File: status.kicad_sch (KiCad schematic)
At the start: 12 parts, among them U7 STP08CP05

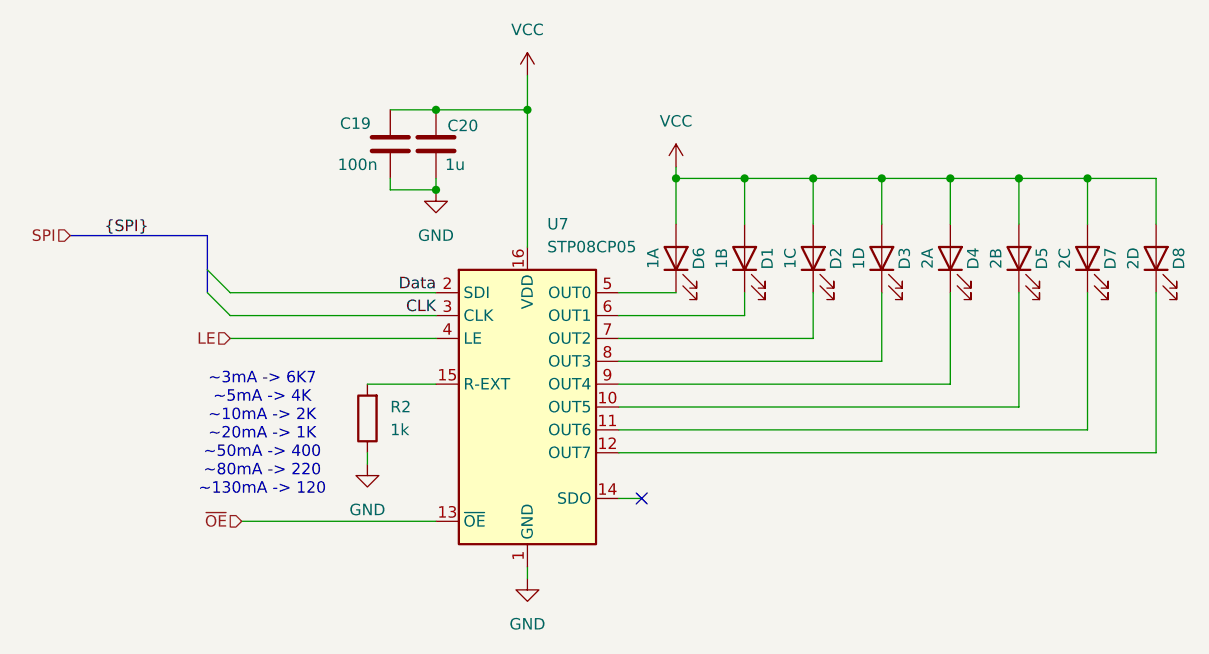
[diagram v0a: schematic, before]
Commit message: Resolve ERC warnings
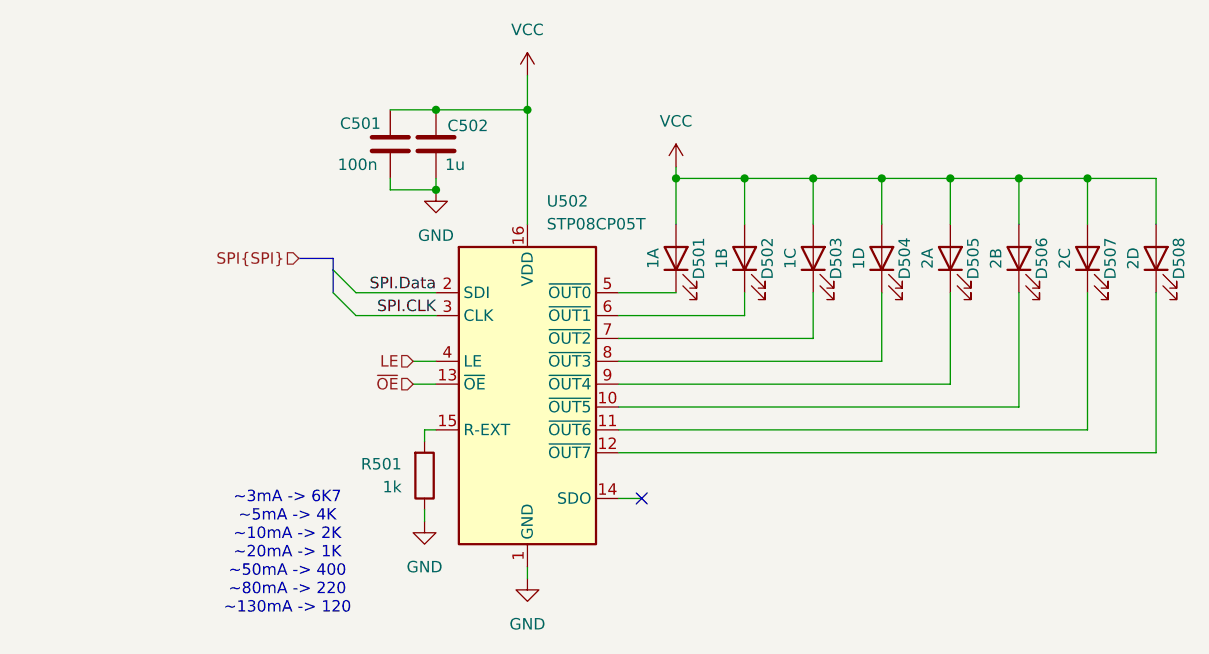
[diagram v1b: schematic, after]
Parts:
- removed U7: STP08CP05, symbol Driver_LED:STP08CP05
- added U502: STP08CP05T, Package_SO:TSSOP-16_4.4x5mm_P0.65mm, symbol Driver_LED:STP08CP05T
- renumbered C19 to C501, C20 to C502, D6 to D501, D1 to D502, D2 to D503, D3 to D504, D4 to D505, D5 to D506, D7 to D507, D8 to D508, R2 to R501
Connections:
- net GND: now also U502.1 (GND)
- net LE: now also U502.4 (LE)
- net VCC: now also U502.16 (VDD)
- net ~{OE}: now also U502.13 (~{OE})
- net at D501.1 (K): now also U502.5 (~{OUT0})
- net at D503.1 (K): now also U502.7 (~{OUT2})
- net at D508.1 (K): now also U502.12 (~{OUT7})
- net at D506.1 (K): now also U502.10 (~{OUT5})
- net at D504.1 (K): now also U502.8 (~{OUT3})
- net at D505.1 (K): now also U502.9 (~{OUT4})
- net at R501.2: now also U502.15 (R-EXT)
- net at D507.1 (K): now also U502.11 (~{OUT6})
- net at D502.1 (K): now also U502.6 (~{OUT1})
- new net SPI.CLK: U502.3 (CLK)
- new net SPI.Data: U502.2 (SDI)
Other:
- moved on the sheet: R501

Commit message: Add Testpoints
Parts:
- added TP12: LE, symbol Connector:TestPoint
- added TP13: ~{OE}, symbol Connector:TestPoint
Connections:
- net LE: now also TP12.1
- net ~{OE}: now also TP13.1
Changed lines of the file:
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@@
+	)
+	(junction
+		(at 110.49 96.52)
+		(diameter 0)
+		(color 0 0 0 0)
 	)
 	(junction
@@
 	)
 	(junction
+		(at 110.49 93.98)
+		(diameter 0)
+		(color 0 0 0 0)
+	)
+	(junction
 		(at 120.65 74.93)
 		(diameter 0)
@@
 	(wire
 		(pts
-			(xy 118.11 96.52) (xy 120.65 96.52)
+			(xy 107.95 96.52) (xy 110.49 96.52)
 		)
 		(stroke
@@
 	(wire
 		(pts
-			(xy 118.11 93.98) (xy 120.65 93.98)
+			(xy 107.95 93.98) (xy 110.49 93.98)
 		)
 		(stroke
@@
 	(wire
 		(pts
+			(xy 110.49 96.52) (xy 120.65 96.52)
+		)
+		(stroke
+			(width 0)
+			(type default)
+		)
+	)
+	(wire
+		(pts
 			(xy 119.38 101.6) (xy 120.65 101.6)
+		)
+		(stroke
+			(width 0)
+			(type default)
+		)
+	)
+	(wire
+		(pts
+			(xy 110.49 93.98) (xy 120.65 93.98)
 		)
 		(stroke
@@
 	(hierarchical_label "LE"
 		(shape input)
-		(at 118.11 93.98 180)
+		(at 107.95 93.98 180)
 		(effects
 			(font
@@
 	(hierarchical_label "~{OE}"
 		(shape input)
-		(at 118.11 96.52 180)
+		(at 107.95 96.52 180)
 		(effects
 			(font
@@
 	)
 	(symbol
+		(lib_id "Connector:TestPoint")
+		(at 110.49 93.98 0)
+		(unit 1)
+		(exclude_from_sim no)
+		(in_bom yes)
+		(on_board yes)
+		(dnp no)
+		(property "Reference" "TP12"
+			(at 112.014 90.424 0)
+			(effects
+				(font
+					(size 1.27 1.27)
+				)
+				(justify left)
+			)
+		)
+		(property "Value" "LE"
+			(at 112.268 92.71 0)
+			(effects
+				(font
+					(size 1.27 1.27)
+				)
+				(justify left)
+			)
+		)
+		(property "Footprint" ""
+			(at 115.57 93.98 0)
+			(effects
+				(font
+					(size 1.27 1.27)
+				)
+				(hide yes)
+			)
+		)
+		(property "Datasheet" "~"
+			(at 115.57 93.98 0)
+			(effects
+				(font
+					(size 1.27 1.27)
+				)
+				(hide yes)
+			)
+		)
+		(property "Description" "test point"
+			(at 110.49 93.98 0)
+			(effects
+				(font
+					(size 1.27 1.27)
+				)
+				(hide yes)
+			)
+		)
+		(pin "1"
+		)
+		(instances
+			(project "LifeCounter"
+				(path "/16b3e55a-9d75-49bf-a6fe-25414eb3d7da/8c2171b0-d87d-41f8-af80-94d86e99ac21"
+					(reference "TP12")
+					(unit 1)
+				)
+			)
+		)
+	)
+	(symbol
 		(lib_id "Device:LED")
 		(at 162.56 82.55 90)
@@
 					(unit 1)
 				)
+			)
+		)
+	)
+	(symbol
+		(lib_id "Connector:TestPoint")
+		(at 110.49 96.52 180)
+		(unit 1)
+		(exclude_from_sim no)
+		(in_bom yes)
+		(on_board yes)
+		(dnp no)
+		(fields_autoplaced yes)
+		(property "Reference" "TP13"
+			(at 113.03 98.5519 0)
+			(effects
+				(font
+					(size 1.27 1.27)
+				)
+				(justify right)
+			)
+		)
+		(property "Value" "~{OE}"
+			(at 113.03 101.0919 0)
+			(effects
+				(font
+					(size 1.27 1.27)
+				)
+				(justify right)
+			)
+		)
+		(property "Footprint" ""
+			(at 105.41 96.52 0)
+			(effects
+				(font
+					(size 1.27 1.27)
+				)
+				(hide yes)
+			)
+		)
+		(property "Datasheet" "~"
+			(at 105.41 96.52 0)
+			(effects
+				(font
+					(size 1.27 1.27)
+				)
+				(hide yes)
+			)
+		)
+		(property "Description" "test point"
+			(at 110.49 96.52 0)
+			(effects
+				(font
+					(size 1.27 1.27)
+				)
+				(hide yes)
+			)
+		)
+		(pin "1"
+		)
+		(instances
+			(project "LifeCounter"
+				(path "/16b3e55a-9d75-49bf-a6fe-25414eb3d7da/8c2171b0-d87d-41f8-af80-94d86e99ac21"
+					(reference "TP13")
+					(unit 1)
+				)

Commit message: Footprint selection
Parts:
- C501, C502: footprint Capacitor_SMD:C_0805_2012Metric_Pad1.18x1.45mm_HandSolder -> Capacitor_SMD:C_1206_3216Metric_Pad1.33x1.80mm_HandSolder
- D501, D502, D503, D504, D505, D506, D507, D508: footprint LED_SMD:LED_0805_2012Metric_Pad1.15x1.40mm_HandSolder -> LED_SMD:LED_1206_3216Metric_Pad1.42x1.75mm_HandSolder
- R501: footprint Resistor_SMD:R_0805_2012Metric_Pad1.20x1.40mm_HandSolder -> Resistor_SMD:R_1206_3216Metric_Pad1.30x1.75mm_HandSolder
- TP12, TP13: footprint (none) -> TestPoint:TestPoint_Pad_D1.0mm
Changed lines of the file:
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@@
 			)
 		)
-		(property "Footprint" "LED_SMD:LED_0805_2012Metric_Pad1.15x1.40mm_HandSolder"
+		(property "Footprint" "LED_SMD:LED_1206_3216Metric_Pad1.42x1.75mm_HandSolder"
 			(at 147.32 82.55 0)
 			(effects
@@
 			)
 		)
-		(property "Footprint" ""
+		(property "Footprint" "TestPoint:TestPoint_Pad_D1.0mm"
 			(at 115.57 93.98 0)
 			(effects
@@
 			)
 		)
-		(property "Footprint" "LED_SMD:LED_0805_2012Metric_Pad1.15x1.40mm_HandSolder"
+		(property "Footprint" "LED_SMD:LED_1206_3216Metric_Pad1.42x1.75mm_HandSolder"
 			(at 162.56 82.55 0)
 			(effects
@@
 			)
 		)
-		(property "Footprint" "Capacitor_SMD:C_0805_2012Metric_Pad1.18x1.45mm_HandSolder"
+		(property "Footprint" "Capacitor_SMD:C_1206_3216Metric_Pad1.33x1.80mm_HandSolder"
 			(at 121.6152 73.66 0)
 			(effects
@@
 			)
 		)
-		(property "Footprint" "LED_SMD:LED_0805_2012Metric_Pad1.15x1.40mm_HandSolder"
+		(property "Footprint" "LED_SMD:LED_1206_3216Metric_Pad1.42x1.75mm_HandSolder"
 			(at 200.66 82.55 0)
 			(effects
@@
 			)
 		)
-		(property "Footprint" "LED_SMD:LED_0805_2012Metric_Pad1.15x1.40mm_HandSolder"
+		(property "Footprint" "LED_SMD:LED_1206_3216Metric_Pad1.42x1.75mm_HandSolder"
 			(at 185.42 82.55 0)
 			(effects
@@
 			)
 		)
-		(property "Footprint" "LED_SMD:LED_0805_2012Metric_Pad1.15x1.40mm_HandSolder"
+		(property "Footprint" "LED_SMD:LED_1206_3216Metric_Pad1.42x1.75mm_HandSolder"
 			(at 170.18 82.55 0)
 			(effects
@@
 			)
 		)
-		(property "Footprint" "LED_SMD:LED_0805_2012Metric_Pad1.15x1.40mm_HandSolder"
+		(property "Footprint" "LED_SMD:LED_1206_3216Metric_Pad1.42x1.75mm_HandSolder"
 			(at 177.8 82.55 0)
 			(effects
@@
 			)
 		)
-		(property "Footprint" "Resistor_SMD:R_0805_2012Metric_Pad1.20x1.40mm_HandSolder"
+		(property "Footprint" "Resistor_SMD:R_1206_3216Metric_Pad1.30x1.75mm_HandSolder"
 			(at 117.602 106.68 90)
 			(effects
@@
 			)
 		)
-		(property "Footprint" ""
+		(property "Footprint" "TestPoint:TestPoint_Pad_D1.0mm"
 			(at 105.41 96.52 0)
 			(effects
@@
 			)
 		)
-		(property "Footprint" "LED_SMD:LED_0805_2012Metric_Pad1.15x1.40mm_HandSolder"
+		(property "Footprint" "LED_SMD:LED_1206_3216Metric_Pad1.42x1.75mm_HandSolder"
 			(at 193.04 82.55 0)
 			(effects
@@
 			)
 		)
-		(property "Footprint" "Capacitor_SMD:C_0805_2012Metric_Pad1.18x1.45mm_HandSolder"
+		(property "Footprint" "Capacitor_SMD:C_1206_3216Metric_Pad1.33x1.80mm_HandSolder"
 			(at 116.5352 73.66 0)
 			(effects
@@
 			)
 		)
-		(property "Footprint" "LED_SMD:LED_0805_2012Metric_Pad1.15x1.40mm_HandSolder"
+		(property "Footprint" "LED_SMD:LED_1206_3216Metric_Pad1.42x1.75mm_HandSolder"
 			(at 154.94 82.55 0)
 			(effects

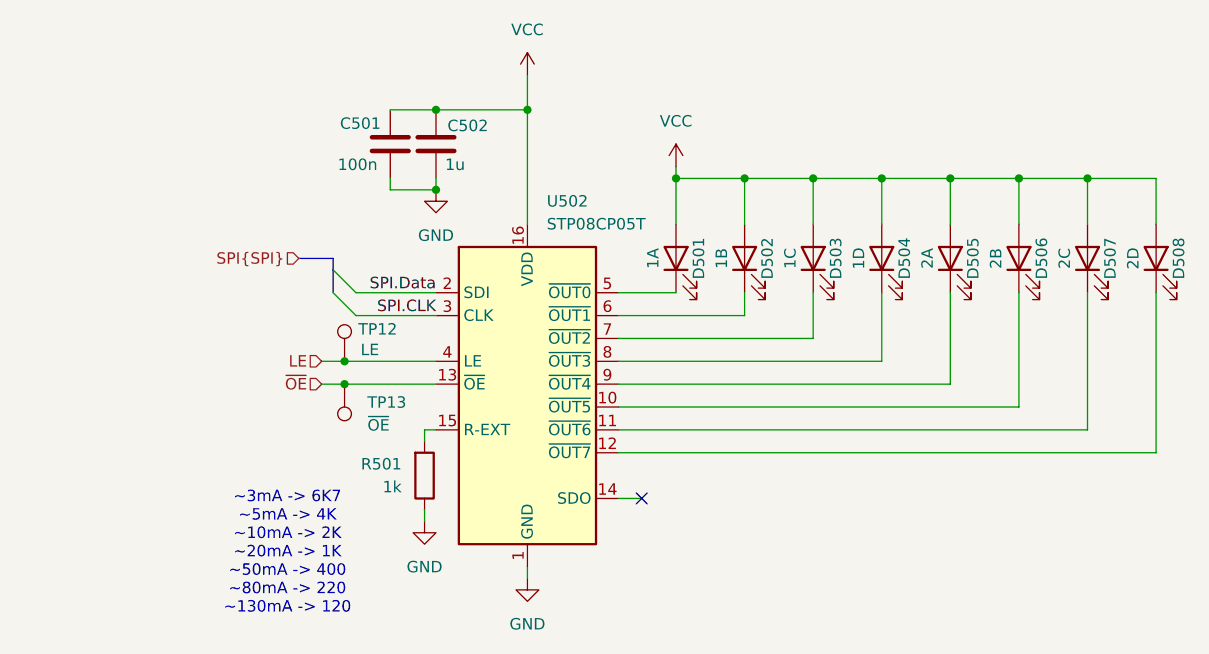
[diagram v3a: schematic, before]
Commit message: Using larger footprint for Status LED driver
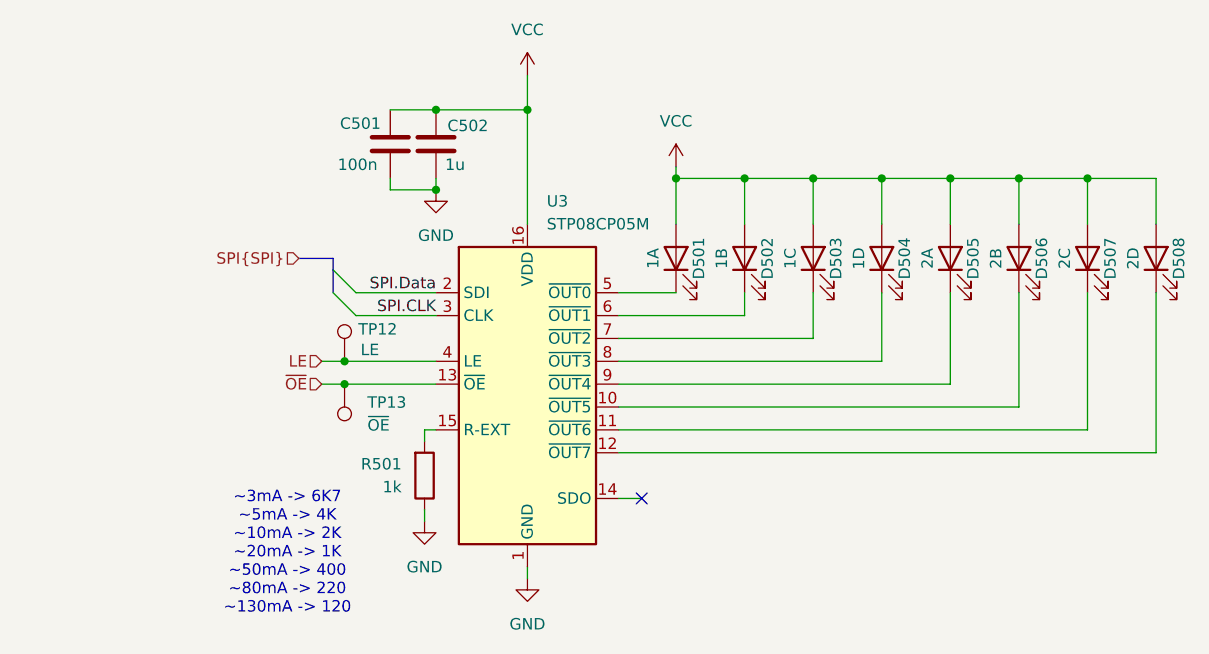
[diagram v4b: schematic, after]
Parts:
- removed U502: STP08CP05T, Package_SO:TSSOP-16_4.4x5mm_P0.65mm, symbol Driver_LED:STP08CP05T
- added U3: STP08CP05M, Package_SO:SOIC-16_3.9x9.9mm_P1.27mm, symbol Driver_LED:STP08CP05M
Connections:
- net GND: now also U3.1 (GND)
- net LE: now also U3.4 (LE)
- net SPI.CLK: now also U3.3 (CLK)
- net SPI.Data: now also U3.2 (SDI)
- net VCC: now also U3.16 (VDD)
- net ~{OE}: now also U3.13 (~{OE})
- net at D501.1 (K): now also U3.5 (~{OUT0})
- net at D503.1 (K): now also U3.7 (~{OUT2})
- net at D508.1 (K): now also U3.12 (~{OUT7})
- net at D506.1 (K): now also U3.10 (~{OUT5})
- net at D507.1 (K): now also U3.11 (~{OUT6})
- net at R501.2: now also U3.15 (R-EXT)
- net at D502.1 (K): now also U3.6 (~{OUT1})
- net at D504.1 (K): now also U3.8 (~{OUT3})
- net at D505.1 (K): now also U3.9 (~{OUT4})
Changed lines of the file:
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@@
-	)
-	(symbol
-		(lib_id "Driver_LED:STP08CP05T")
-		(at 130.81 99.06 0)
-		(unit 1)
-		(exclude_from_sim no)
-		(in_bom yes)
-		(on_board yes)
-		(dnp no)
-		(fields_autoplaced yes)
-		(property "Reference" "U502"
-			(at 132.9533 76.2 0)
-			(effects
-				(font
-					(size 1.27 1.27)
-				)
-				(justify left)
-			)
-		)
-		(property "Value" "STP08CP05T"
-			(at 132.9533 78.74 0)
-			(effects
-				(font
-					(size 1.27 1.27)
-				)
-				(justify left)
-			)
-		)
-		(property "Footprint" "Package_SO:TSSOP-16_4.4x5mm_P0.65mm"
-			(at 130.81 99.06 0)
-			(effects
-				(font
-					(size 1.27 1.27)
-				)
-				(hide yes)
-			)
-		)
-		(property "Datasheet" "https://www.st.com/resource/en/datasheet/stp08cp05.pdf"
-			(at 130.81 99.06 0)
-			(effects
-				(font
-					(size 1.27 1.27)
-				)
-				(hide yes)
-			)
-		)
-		(property "Description" "8-bit constant current LED sink driver, 5..100mA output current, 20V driving capability, 3.0..5.5V power supply, TSSOP-16"
-			(at 130.81 99.06 0)
-			(effects
-				(font
-					(size 1.27 1.27)
-				)
-				(hide yes)
-			)
-		)
-		(pin "3"
-		)
-		(pin "2"
-		)
-		(pin "11"
-		)
-		(pin "4"
-		)
-		(pin "10"
-		)
-		(pin "8"
-		)
-		(pin "13"
-		)
-		(pin "14"
-		)
-		(pin "15"
-		)
-		(pin "16"
-		)
-		(pin "1"
-		)
-		(pin "9"
-		)
-		(pin "7"
-		)
-		(pin "5"
-		)
-		(pin "6"
-		)
-		(pin "12"
-		)
-		(instances
-			(project ""
-				(path "/16b3e55a-9d75-49bf-a6fe-25414eb3d7da/8c2171b0-d87d-41f8-af80-94d86e99ac21"
-					(reference "U502")
-					(unit 1)
-				)
-			)
-		)
 	)
 	(symbol
@@
 					(unit 1)
 				)
+			)
+		)
+	)
+	(symbol
+		(lib_id "Driver_LED:STP08CP05M")
+		(at 130.81 99.06 0)
+		(unit 1)
+		(exclude_from_sim no)
+		(in_bom yes)
+		(on_board yes)
+		(dnp no)
+		(fields_autoplaced yes)
+		(property "Reference" "U3"
+			(at 132.9533 76.2 0)
+			(effects
+				(font
+					(size 1.27 1.27)
+				)
+				(justify left)
+			)
+		)
+		(property "Value" "STP08CP05M"
+			(at 132.9533 78.74 0)
+			(effects
+				(font
+					(size 1.27 1.27)
+				)
+				(justify left)
+			)
+		)
+		(property "Footprint" "Package_SO:SOIC-16_3.9x9.9mm_P1.27mm"
+			(at 130.81 99.06 0)
+			(effects
+				(font
+					(size 1.27 1.27)
+				)
+				(hide yes)
+			)
+		)
+		(property "Datasheet" "https://www.st.com/resource/en/datasheet/stp08cp05.pdf"
+			(at 130.81 99.06 0)
+			(effects
+				(font
+					(size 1.27 1.27)
+				)
+				(hide yes)
+			)
+		)
+		(property "Description" "8-bit constant current LED sink driver, 5..100mA output current, 20V driving capability, 3.0..5.5V power supply, SOIC-16"
+			(at 130.81 99.06 0)
+			(effects
+				(font
+					(size 1.27 1.27)
+				)
+				(hide yes)
+			)
+		)
+		(pin "4"
+		)
+		(pin "9"
+		)
+		(pin "2"
+		)
+		(pin "3"
+		)
+		(pin "1"
+		)
+		(pin "6"
+		)
+		(pin "14"
+		)
+		(pin "10"
+		)
+		(pin "7"
+		)
+		(pin "16"
+		)
+		(pin "15"
+		)
+		(pin "8"
+		)
+		(pin "13"
+		)
+		(pin "11"
+		)
+		(pin "5"
+		)
+		(pin "12"
+		)
+		(instances
+			(project ""
+				(path "/16b3e55a-9d75-49bf-a6fe-25414eb3d7da/8c2171b0-d87d-41f8-af80-94d86e99ac21"
+					(reference "U3")
+					(unit 1)
+				)
